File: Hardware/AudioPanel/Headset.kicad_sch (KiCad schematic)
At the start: 1 part, among them J1 8P8C_Shielded

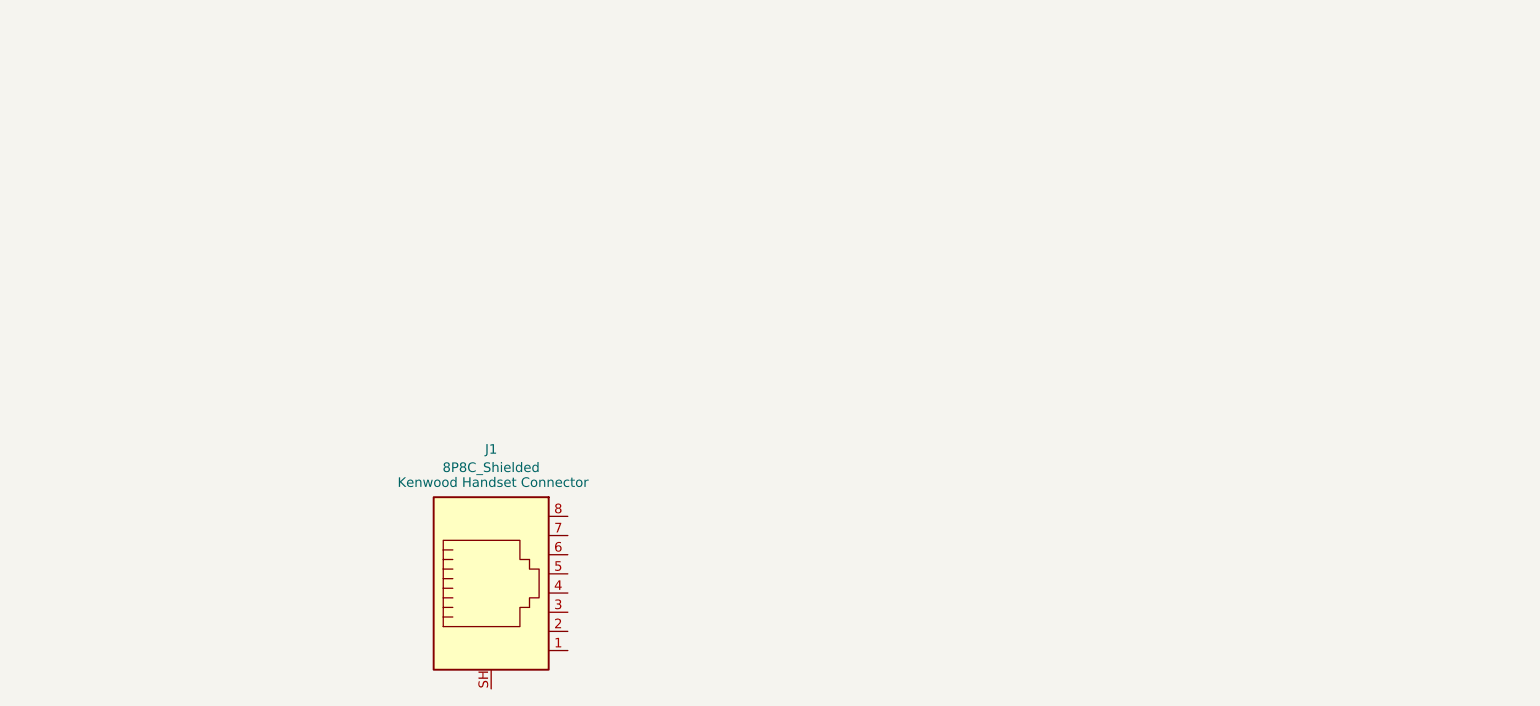
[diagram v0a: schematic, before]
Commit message: Added headphone and speaker jack interfaces
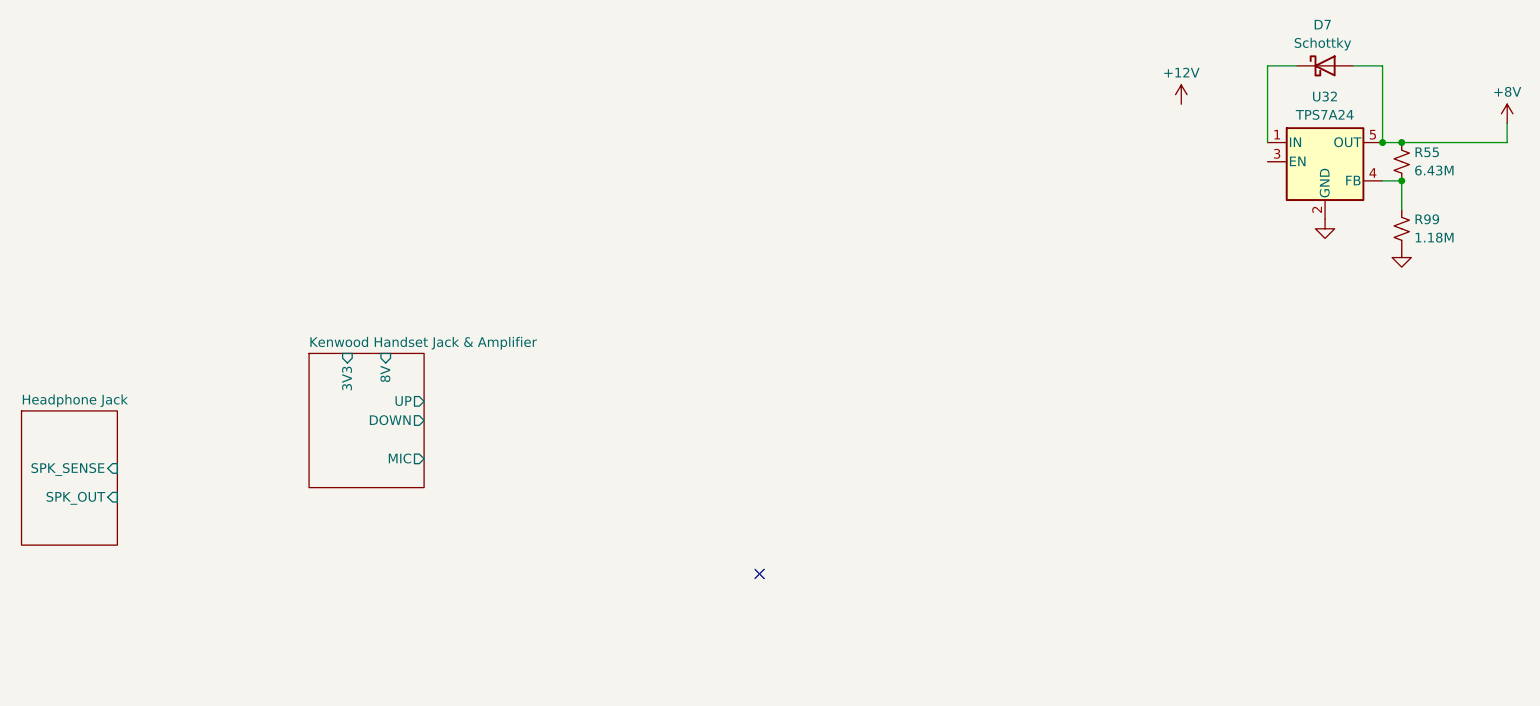
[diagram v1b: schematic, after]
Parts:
- removed J1: 8P8C_Shielded, symbol Connector:8P8C_Shielded
- added D7: Schottky, symbol Device:D_Schottky
- added R55: 6.43M, symbol Device:R_Small_US
- added R99: 1.18M, symbol Device:R_Small_US
- added U32: TPS7A24, Package_TO_SOT_SMD:SOT-23-5, symbol Regulator_Linear:AP131-29
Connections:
- new net: D7.1 (K), U32.1 (IN)
- new net: R55.2, R99.1, U32.4 (FB)
- new net +8V: D7.2 (A), R55.1, U32.5 (OUT)
- new net GND: R99.2, U32.2 (GND)
- no-connect marks 0 -> 1
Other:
- added sheet Headphone Jack (HeadphoneJack.kicad_sch)
- added sheet Kenwood Handset Jack & Amplifier (HandsetJackAmp.kicad_sch)

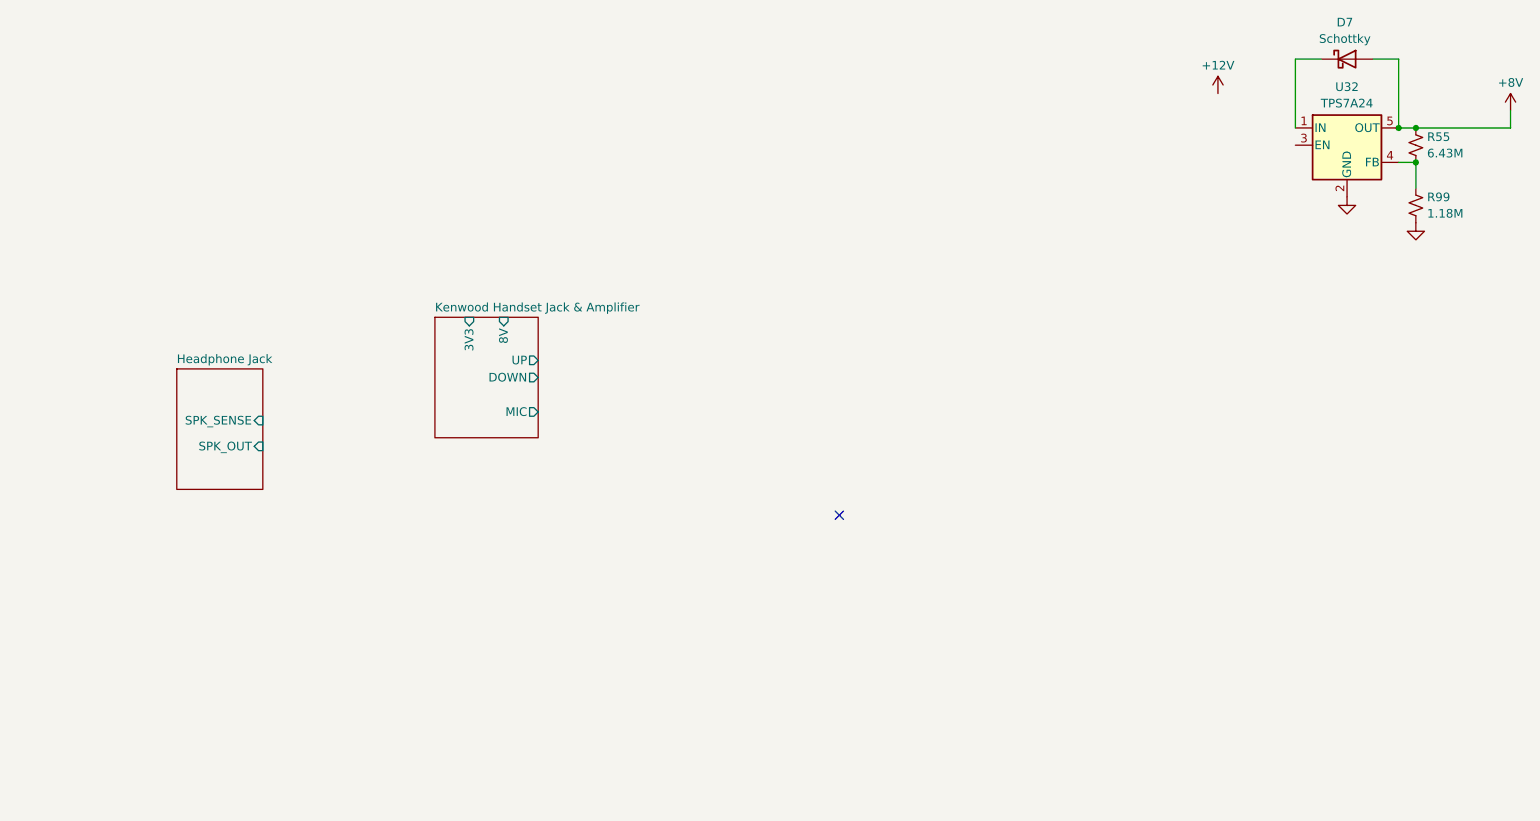
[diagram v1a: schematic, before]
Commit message: Added crosspoints for each connector
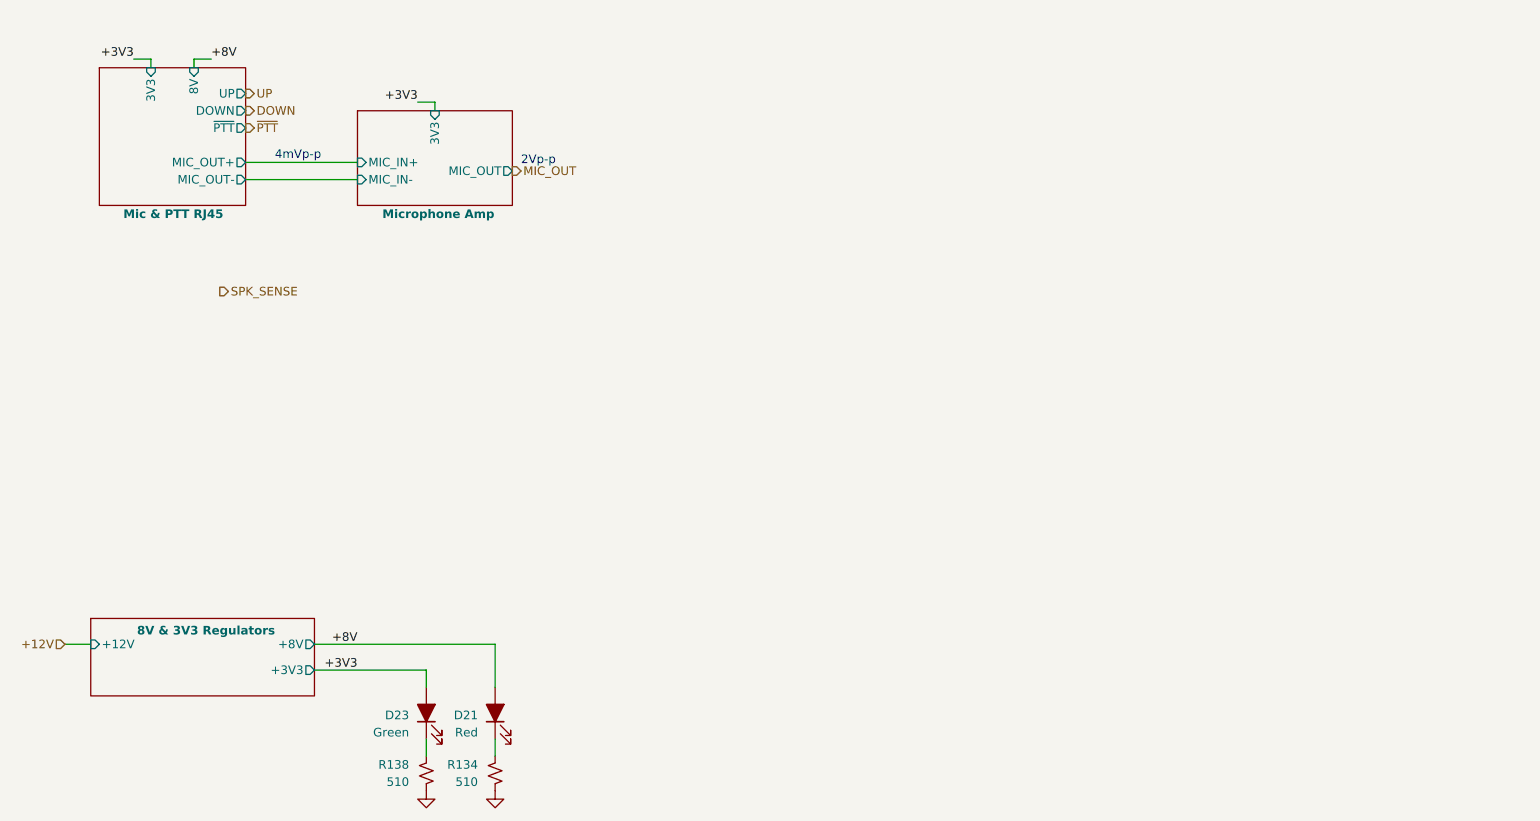
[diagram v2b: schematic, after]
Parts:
- removed D7: Schottky, symbol Device:D_Schottky
- removed R55: 6.43M, symbol Device:R_Small_US
- removed R99: 1.18M, symbol Device:R_Small_US
- removed U32: TPS7A24, Package_TO_SOT_SMD:SOT-23-5, symbol Regulator_Linear:AP131-29
- added D21: Red, LED_THT:LED_D5.0mm, symbol Device:LED_Filled
- added D23: Green, LED_THT:LED_D5.0mm, symbol Device:LED_Filled
- added R134, R138: 510, Resistor_SMD:R_0603_1608Metric_Pad0.98x0.95mm_HandSolder, symbol Device:R_Small_US
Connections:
- net +8V: now also D21.2 (A)
- net GND: now also R134.1, R138.1
- new net: D21.1 (K), R134.2
- new net: D23.1 (K), R138.2
- new net +3V3: D23.2 (A)
- no-connect marks 1 -> 0
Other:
- sheet Kenwood Handset Jack & Amplifier renamed Mic & PTT RJ45
- removed sheet Headphone Jack
- added sheet 8V & 3V3 Regulators (12-8-3Reg.kicad_sch)
- added sheet Microphone Amp (MicAmp.kicad_sch)
- sheet Mic & PTT RJ45 ports: added MIC_OUT+, MIC_OUT-, ~{PTT}; removed MIC
- note added: "2Vp-p"
- note added: "4mVp-p"

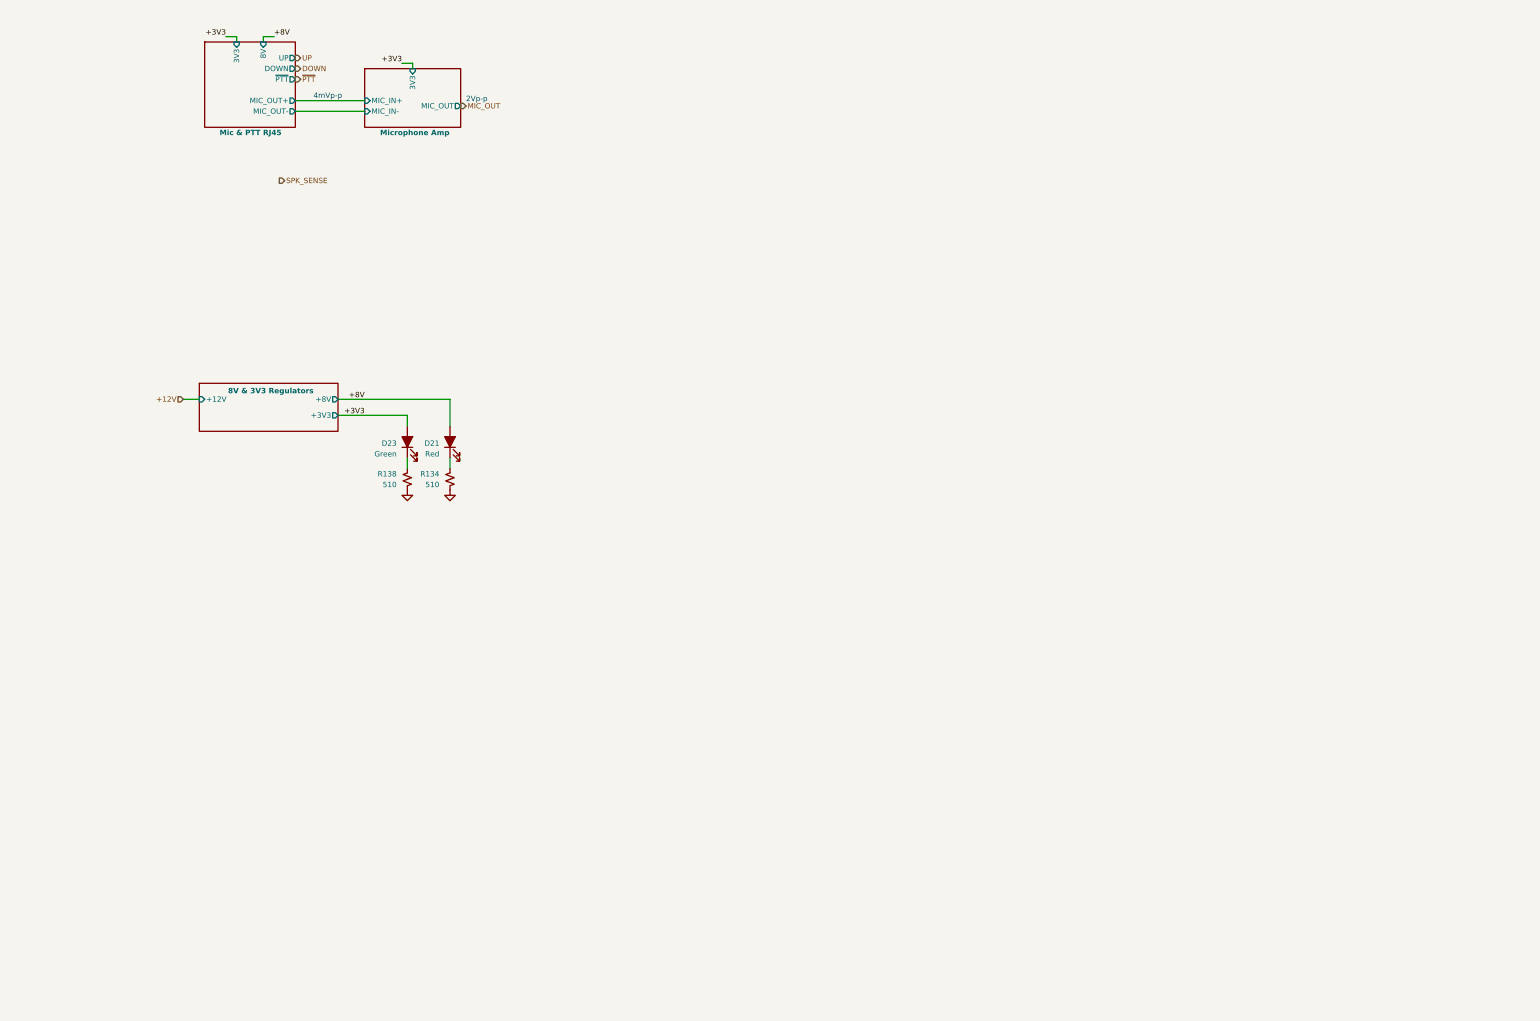
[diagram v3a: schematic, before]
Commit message: Added group labels
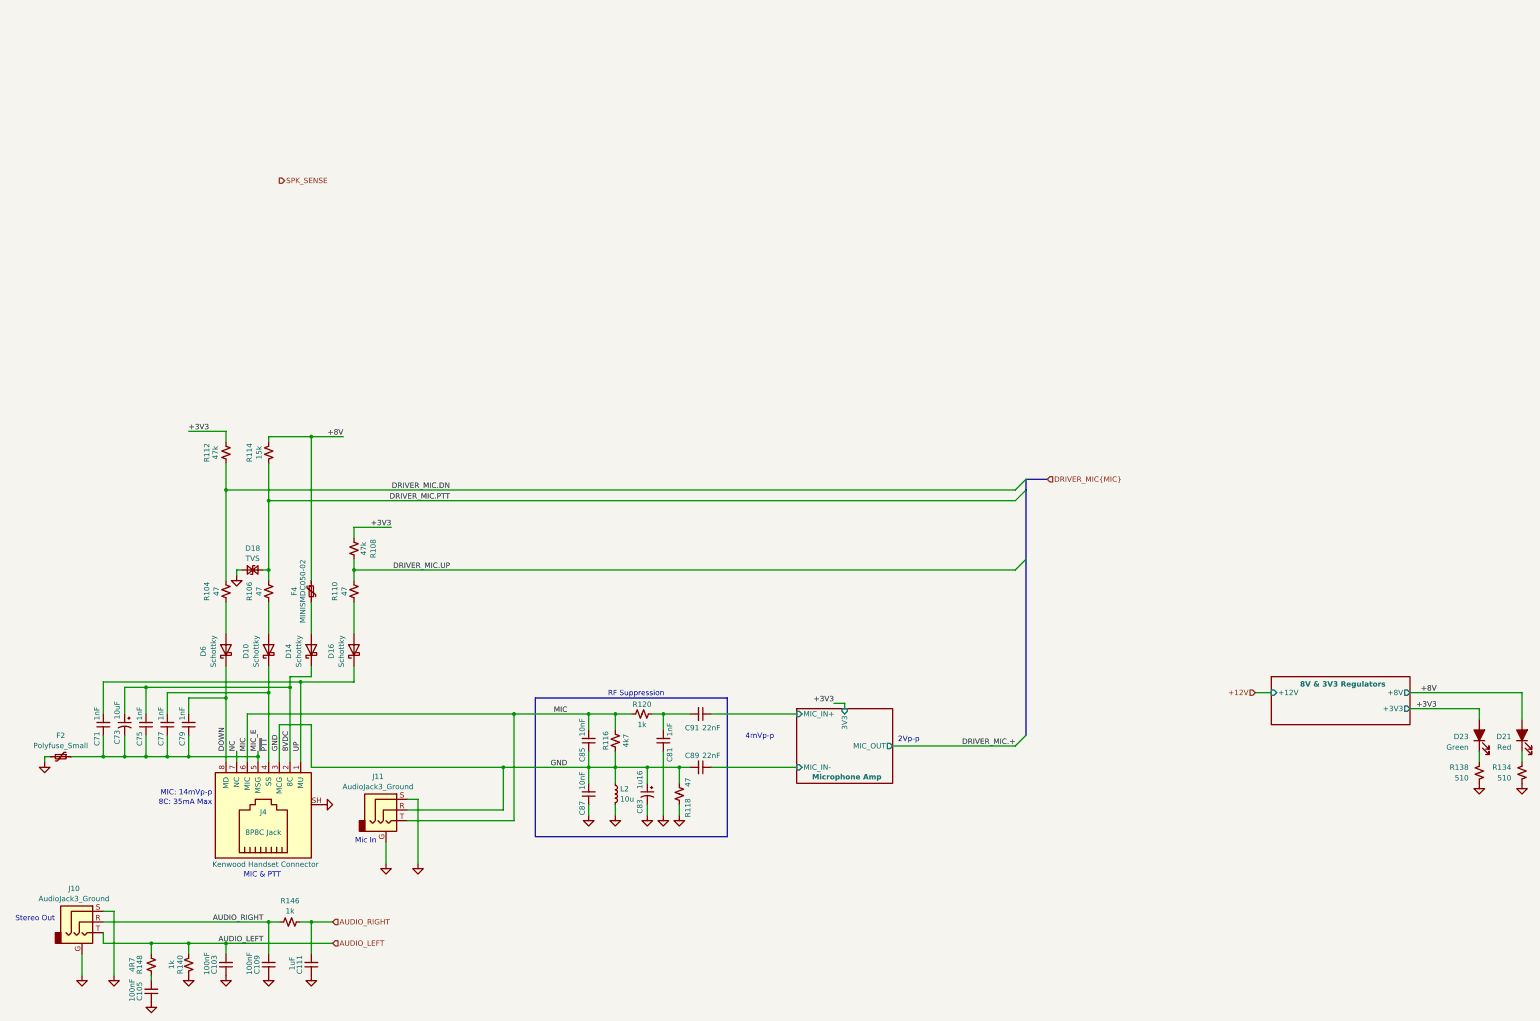
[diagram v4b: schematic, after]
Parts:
- added C103, C105, C109: 100nF, symbol Device:C_Small
- added C111: 1uF, symbol Device:C_Small
- added C71, C75, C77, C79, C81: 1nF, symbol Device:C_Small
- added C73: 10uF, symbol Device:C_Polarized_Small_US
- added C83: 1u16, symbol Device:C_Polarized_Small_US
- added C85, C87: 10nF, symbol Device:C_Small
- added C89, C91: 22nF, symbol Device:C_Small
- added D10, D14, D16, D6: Schottky, symbol Device:D_Schottky
- added D18: TVS, symbol Device:D_TVS_Small
- added F2: Polyfuse_Small, symbol Device:Polyfuse_Small
- added F4: MINISMDC050-02, symbol Device:Polyfuse_Small
- added J10, J11: AudioJack3_Ground, symbol Connector_Audio:AudioJack3_Ground
- added J4: 8P8C Jack, symbol Connector:8P8C_Shielded
- added L2: 10u, symbol Device:L_Small
- added R104, R106, R110, R118: 47, symbol Device:R_Small_US
- added R108, R112: 47k, symbol Device:R_Small_US
- added R114: 15k, symbol Device:R_Small_US
- added R116: 4k7, symbol Device:R_Small_US
- added R120, R140, R146: 1k, symbol Device:R_Small_US
- added R148: 4R7, symbol Device:R_Small_US
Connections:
- net +3V3: now also R108.2, R112.2
- net +8V: now also F4.1, R114.2
- net DOWN: now also C79.2, D6.1 (K), J4.8 (MD)
- net GND: now also C103.1, C105.1, C109.1, C111.1, C81.1, C83.1, C83.2, C85.1, C87.1, C87.2, C89.2, D18.1 (A1), F2.2, J10.G, J10.S, J11.G, J11.R, J11.S, J4.3 (MCG), J4.SH, L2.1, L2.2, R116.2, R118.1, R118.2, R140.2
- net UP: now also C71.2, D16.1 (K), J4.1 (MU)
- net ~{PTT}: now also C77.2, D10.1 (K), J4.4 (SS)
- new net: D10.2 (A), R106.2
- new net: D16.2 (A), R110.2
- new net: C105.2, R148.1
- new net: C81.2, C91.2, R120.1
- new net: D14.2 (A), F4.2
- new net: D6.2 (A), R104.2
- new net 8VDC: C73.1, C75.2, D14.1 (K), J4.2 (8C)
- new net AUDIO_LEFT: C103.2, J10.T, R140.1, R148.2
- new net AUDIO_RIGHT: C109.2, C111.2, J10.R, R146.1, R146.2
- new net DRIVER_MIC.DN: R104.1, R112.1
- new net DRIVER_MIC.PTT: D18.2 (A2), R106.1, R114.1
- new net DRIVER_MIC.UP: R108.1, R110.1
- new net MIC: C85.2, J11.T, J4.6 (MIC), R116.1, R120.2
- new net MIC_E: C71.1, C73.2, C75.1, C77.1, C79.1, F2.1, J4.5 (MSG)
- new net Microphone Amp/MIC_IN+: C91.1
- new net Microphone Amp/MIC_IN-: C89.1
- new net NC: J4.7 (NC)
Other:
- removed sheet Mic & PTT RJ45
- note added: "8C: 35mA Max"
- note added: "MIC & PTT"
- note added: "MIC: 14mVp-p"
- note added: "Mic In"
- note added: "RF Suppression"
- note added: "Stereo Out"
- moved on the sheet: D21, D23, R134, R138
